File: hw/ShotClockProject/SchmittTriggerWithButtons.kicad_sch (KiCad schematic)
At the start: 13 parts, among them SW3 SW_SPST, SW4 SW_SPST, SW5 SW_SPST, U3 M74HC14YRM13TR

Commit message: Finished rough layout of PCB (ready for review)
Changed battery polarity to match the batteries I have.
Added power led to voltage regulator
Removed old comments from schematic
Gave all footprints a 3D model
Replaced batttery footprint with a SMD JST 3 pins horizontal connector
Finished rough placement of components
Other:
- note removed: "Pull-up resistor to 3v3 (47k) and smaller resistor (10k) to create path of least resistance. Is this assumption correct, or is the extra 10k not needed? And does it matter that there is a voltage devision on pin 1 of the switch? (I dont think so, since 3v3 will flow to the right if switch is not pressed?) Current limit here should not matter to much right?"
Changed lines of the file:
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@@
     (effects (font (size 2.5 2.5) (color 255 0 0 1)) (justify left bottom))
-  )
-  (text "Pull-up resistor to 3v3 (47k)\nand smaller resistor (10k) to \ncreate path of least resistance.\nIs this assumption correct, \nor is the extra 10k not needed?\nAnd does it matter that there is a \nvoltage devision on pin 1 of the switch?\n(I dont think so, since 3v3 will flow \nto the right if switch is not pressed?)\nCurrent limit here should not matter to much right?"
-    (at 107.95 71.12 0)
-    (effects (font (size 1.27 1.27)) (justify left bottom))
   )
   (hierarchical_label "button3_out" (shape output) (at 205.74 82.55 0) (fields_autoplaced)

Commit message: First feedback round from Luc on schematic
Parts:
- removed R22, R24, R26: 47k, Resistor_SMD:R_0402_1005Metric, symbol Device:R
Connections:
- net +3.3V: now also SW3.1 (A), SW4.1 (A), SW5.1 (A)
- net GND: now also R23.1, R25.1, R27.1; no longer SW3.2 (B), SW4.2 (B), SW5.2 (B)
- net at C4.1, R23.2, U3.1 (1A): now also SW3.2 (B)
- net at C4.1, R25.2, U3.3 (2A): now also SW4.2 (B)
- net at C4.1, R27.2, U3.5 (3A): now also SW5.2 (B)
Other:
- moved on the sheet: R23, R25, R27, SW3, SW4, SW5

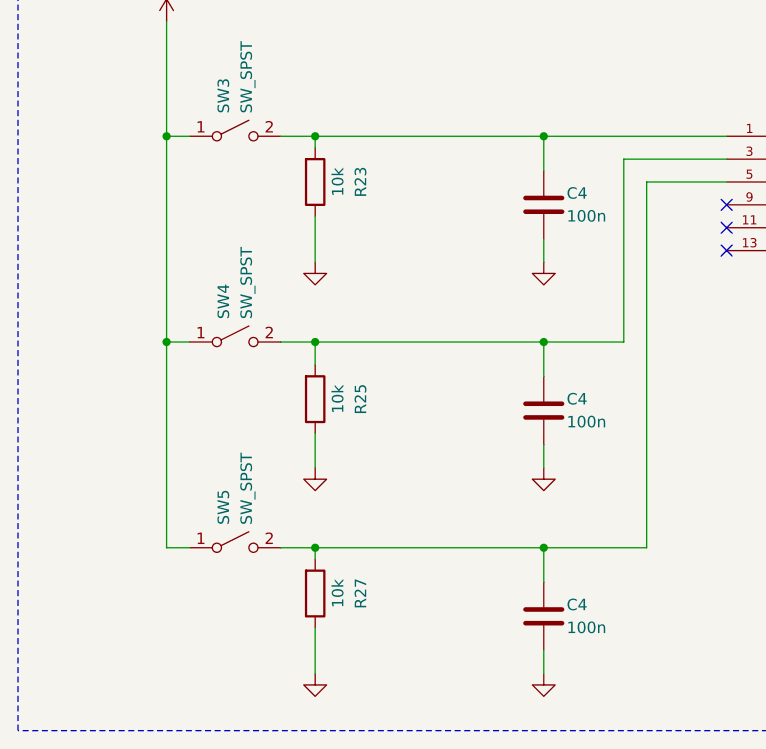
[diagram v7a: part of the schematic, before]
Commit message: Finshed both schematics
- LED driving transistors are placed
- All connectors on segment display PCB are placed
- All schematic references have been re-configured (autosort on Y axis)
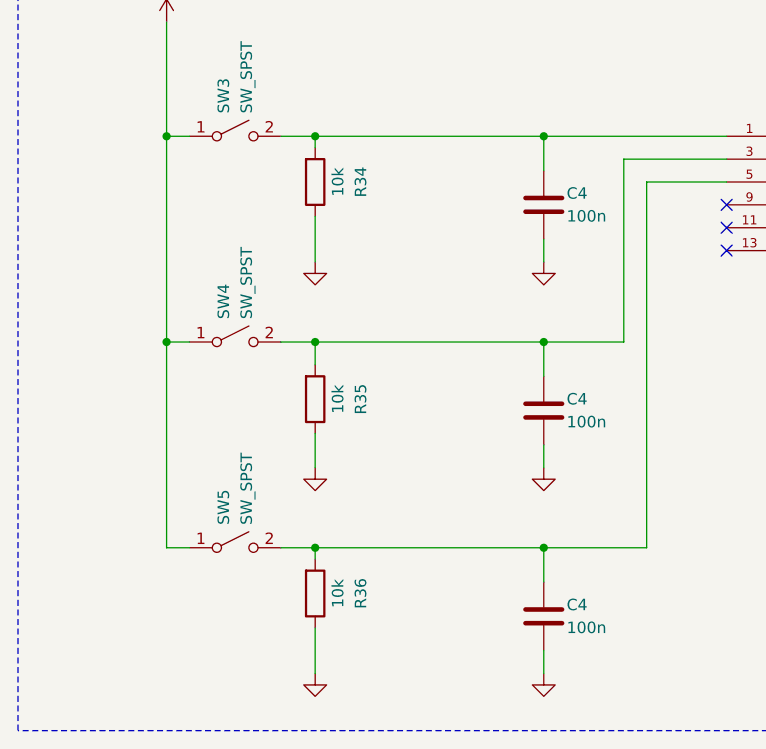
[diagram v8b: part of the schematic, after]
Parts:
- renumbered R23 to R34, R25 to R35, R27 to R36
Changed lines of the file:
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@@
         )
         (path "/5fd859aa-754d-49c2-9762-3f7ebe3bb64c/1ce26b90-d7f5-4886-998a-a021d351eec6"
-          (reference "U4") (unit 1)
+          (reference "U5") (unit 1)
         )
       )
@@
         )
         (path "/5fd859aa-754d-49c2-9762-3f7ebe3bb64c/1ce26b90-d7f5-4886-998a-a021d351eec6"
-          (reference "C22") (unit 1)
+          (reference "C28") (unit 1)
         )
       )
@@
   (symbol (lib_id "Device:R") (at 113.03 106.68 0) (mirror x) (unit 1)
     (in_bom yes) (on_board yes) (dnp no)
-    (property "Reference" "R25" (at 118.11 106.68 90)
+    (property "Reference" "R35" (at 118.11 106.68 90)
       (effects (font (size 1.27 1.27)))
     )
@@
       (project "ShotClockProject"
         (path "/5fd859aa-754d-49c2-9762-3f7ebe3bb64c/1ce26b90-d7f5-4886-998a-a021d351eec6"
-          (reference "R25") (unit 1)
+          (reference "R35") (unit 1)
         )
       )
@@
         )
         (path "/5fd859aa-754d-49c2-9762-3f7ebe3bb64c/1ce26b90-d7f5-4886-998a-a021d351eec6"
-          (reference "#PWR052") (unit 1)
+          (reference "#PWR069") (unit 1)
         )
       )
@@
         )
         (path "/5fd859aa-754d-49c2-9762-3f7ebe3bb64c/1ce26b90-d7f5-4886-998a-a021d351eec6"
-          (reference "#PWR056") (unit 1)
+          (reference "#PWR073") (unit 1)
         )
       )
@@
         )
         (path "/5fd859aa-754d-49c2-9762-3f7ebe3bb64c/1ce26b90-d7f5-4886-998a-a021d351eec6"
-          (reference "#PWR057") (unit 1)
+          (reference "#PWR074") (unit 1)
         )
       )
@@
         )
         (path "/5fd859aa-754d-49c2-9762-3f7ebe3bb64c/1ce26b90-d7f5-4886-998a-a021d351eec6"
-          (reference "C24") (unit 1)
+          (reference "C30") (unit 1)
         )
       )
@@
         )
         (path "/5fd859aa-754d-49c2-9762-3f7ebe3bb64c/1ce26b90-d7f5-4886-998a-a021d351eec6"
-          (reference "#PWR059") (unit 1)
+          (reference "#PWR076") (unit 1)
         )
       )
@@
         )
         (path "/5fd859aa-754d-49c2-9762-3f7ebe3bb64c/1ce26b90-d7f5-4886-998a-a021d351eec6"
-          (reference "#PWR053") (unit 1)
+          (reference "#PWR070") (unit 1)
         )
       )
@@
   (symbol (lib_id "Device:R") (at 113.03 82.55 0) (mirror x) (unit 1)
     (in_bom yes) (on_board yes) (dnp no)
-    (property "Reference" "R23" (at 118.11 82.55 90)
+    (property "Reference" "R34" (at 118.11 82.55 90)
       (effects (font (size 1.27 1.27)))
     )
@@
       (project "ShotClockProject"
         (path "/5fd859aa-754d-49c2-9762-3f7ebe3bb64c/1ce26b90-d7f5-4886-998a-a021d351eec6"
-          (reference "R23") (unit 1)
+          (reference "R34") (unit 1)
         )
       )
@@
         )
         (path "/5fd859aa-754d-49c2-9762-3f7ebe3bb64c/1ce26b90-d7f5-4886-998a-a021d351eec6"
-          (reference "#PWR054") (unit 1)
+          (reference "#PWR071") (unit 1)
         )
       )
@@
         )
         (path "/5fd859aa-754d-49c2-9762-3f7ebe3bb64c/1ce26b90-d7f5-4886-998a-a021d351eec6"
-          (reference "#PWR060") (unit 1)
+          (reference "#PWR077") (unit 1)
         )
       )
@@
         )
         (path "/5fd859aa-754d-49c2-9762-3f7ebe3bb64c/1ce26b90-d7f5-4886-998a-a021d351eec6"
-          (reference "C23") (unit 1)
+          (reference "C29") (unit 1)
         )
       )
@@
         )
         (path "/5fd859aa-754d-49c2-9762-3f7ebe3bb64c/1ce26b90-d7f5-4886-998a-a021d351eec6"
-          (reference "#PWR055") (unit 1)
+          (reference "#PWR072") (unit 1)
         )
       )
@@
         )
         (path "/5fd859aa-754d-49c2-9762-3f7ebe3bb64c/1ce26b90-d7f5-4886-998a-a021d351eec6"
-          (reference "#PWR058") (unit 1)
+          (reference "#PWR075") (unit 1)
         )
       )
@@
   (symbol (lib_id "Device:R") (at 113.03 128.27 0) (mirror x) (unit 1)
     (in_bom yes) (on_board yes) (dnp no)
-    (property "Reference" "R27" (at 118.11 128.27 90)
+    (property "Reference" "R36" (at 118.11 128.27 90)
       (effects (font (size 1.27 1.27)))
     )
@@
       (project "ShotClockProject"
         (path "/5fd859aa-754d-49c2-9762-3f7ebe3bb64c/1ce26b90-d7f5-4886-998a-a021d351eec6"
-          (reference "R27") (unit 1)
-        )
-      )
+          (reference "R36") (unit 1)
+        )
+      )
